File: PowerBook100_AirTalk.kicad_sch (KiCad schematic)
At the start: 41 parts, among them J1 5-104652-2, J2 PRG_HDR, Q1 BSS138, SW1 RST, U1 TashTalk, U2 TXB0104PWR, U3 AMS1117-3.3, U4 ESP32-WROOM-32DM113DH6400PH3Q0, U5 74LVC2G125

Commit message: More mods
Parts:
- removed TP1: RX_PB, TestPoint:TestPoint_Pad_2.0x2.0mm, symbol Connector:TestPoint
- removed TP2: TX_PB, TestPoint:TestPoint_Pad_2.0x2.0mm, symbol Connector:TestPoint
- removed TP3: RTS_PB, TestPoint:TestPoint_Pad_2.0x2.0mm, symbol Connector:TestPoint
- added R17, R18, R19: 0, Resistor_SMD:R_0805_2012Metric, symbol Device:R
- C1, C11, C2, C3, C4, C5, C7: footprint Capacitor_SMD:CP_Elec_6.3x7.7 -> Capacitor_SMD:C_1206_3216Metric
- J2: footprint Connector_Samtec_HPM_THT:Samtec_HPM-03-01-x-S_Straight_1x03_Pitch5.08mm -> Connector_PinHeader_2.00mm:PinHeader_1x03_P2.00mm_Vertical_SMD_Pin1Right
- R12: value 0 -> R
- U1: footprint Package_DIP:DIP-8_W7.62mm -> Package_SO:SOIC-8-1EP_3.9x4.9mm_P1.27mm_EP2.29x3mm
- U3: footprint Package_TO_SOT_SMD:SOT-223-3_TabPin2 -> Package_TO_SOT_SMD:TO-252-3_TabPin2
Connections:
- net +3.3V: now also R12.1
- net +5V: now also R17.2, R18.2; no longer J1.5, R12.1
- net LT_TX_33: now also R12.2
- net MODEM_INSERT: no longer R12.2
- net PB_CTS: now reaches J1.14
- net PB_CTS: now also R19.1
- net MODEM_5v: now reaches J1.18
- net MODEM_5v: now also J1.20, R17.1
- net at R11.2, U2.5 (A4): now also R19.2
- new net ALWAYS_ON_5V: J1.5, R18.1
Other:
- note added: "Puoi usare SOIC8"
- moved on the sheet: R11

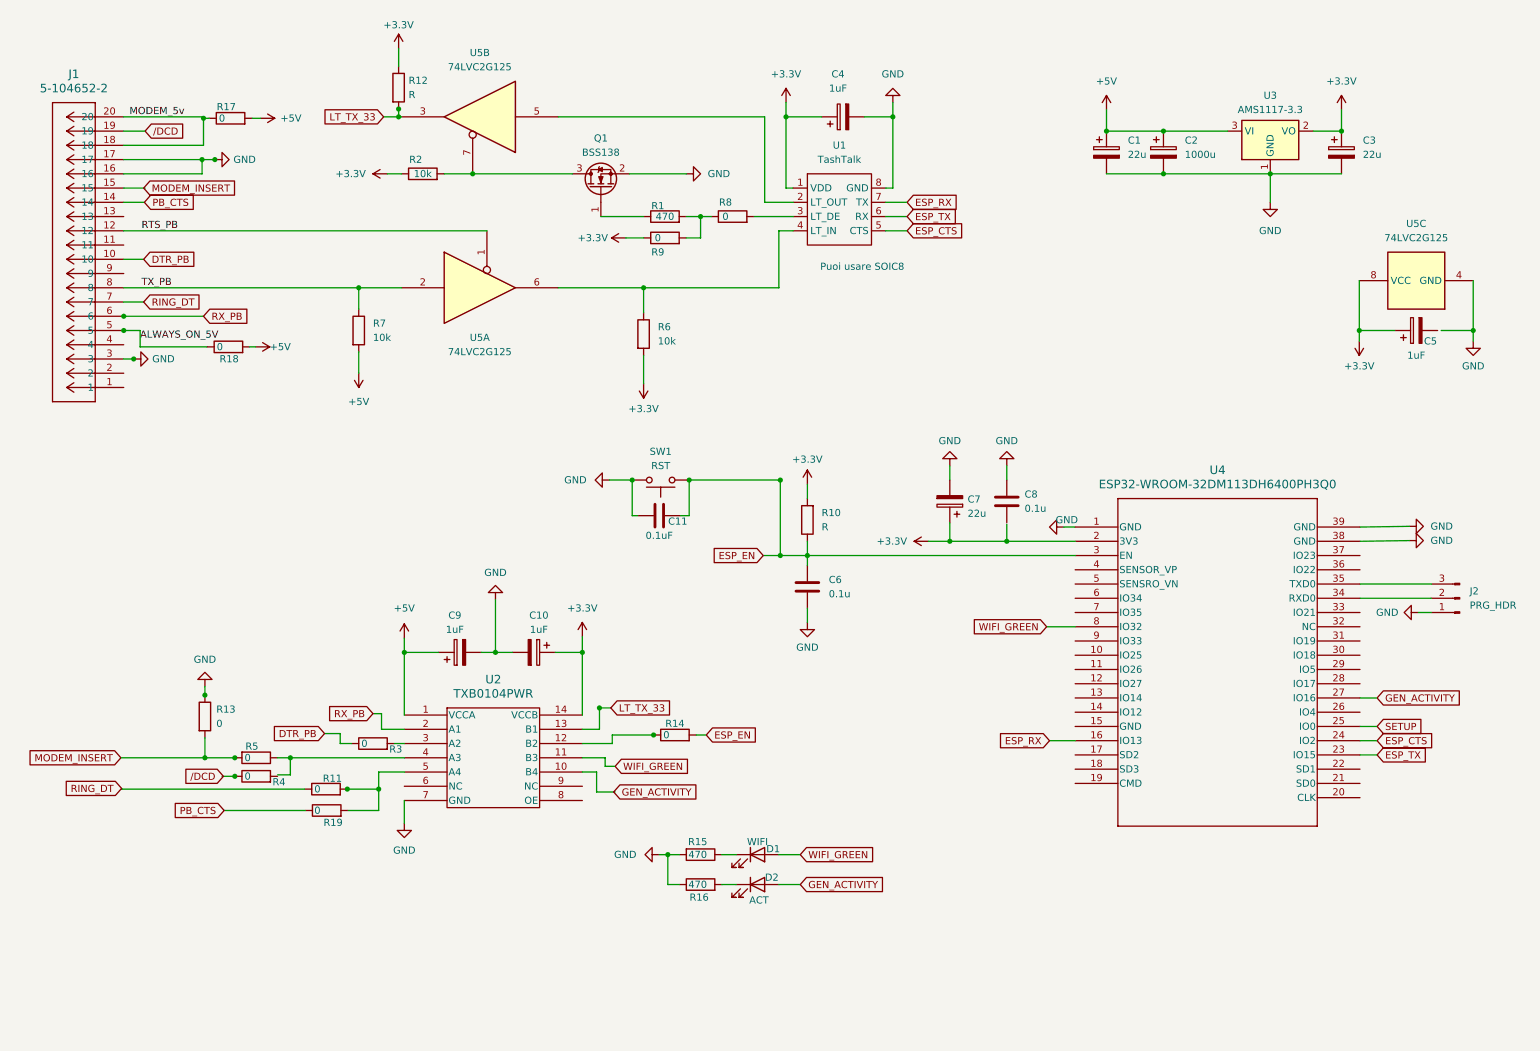
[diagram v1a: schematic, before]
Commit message: Add PCB layout
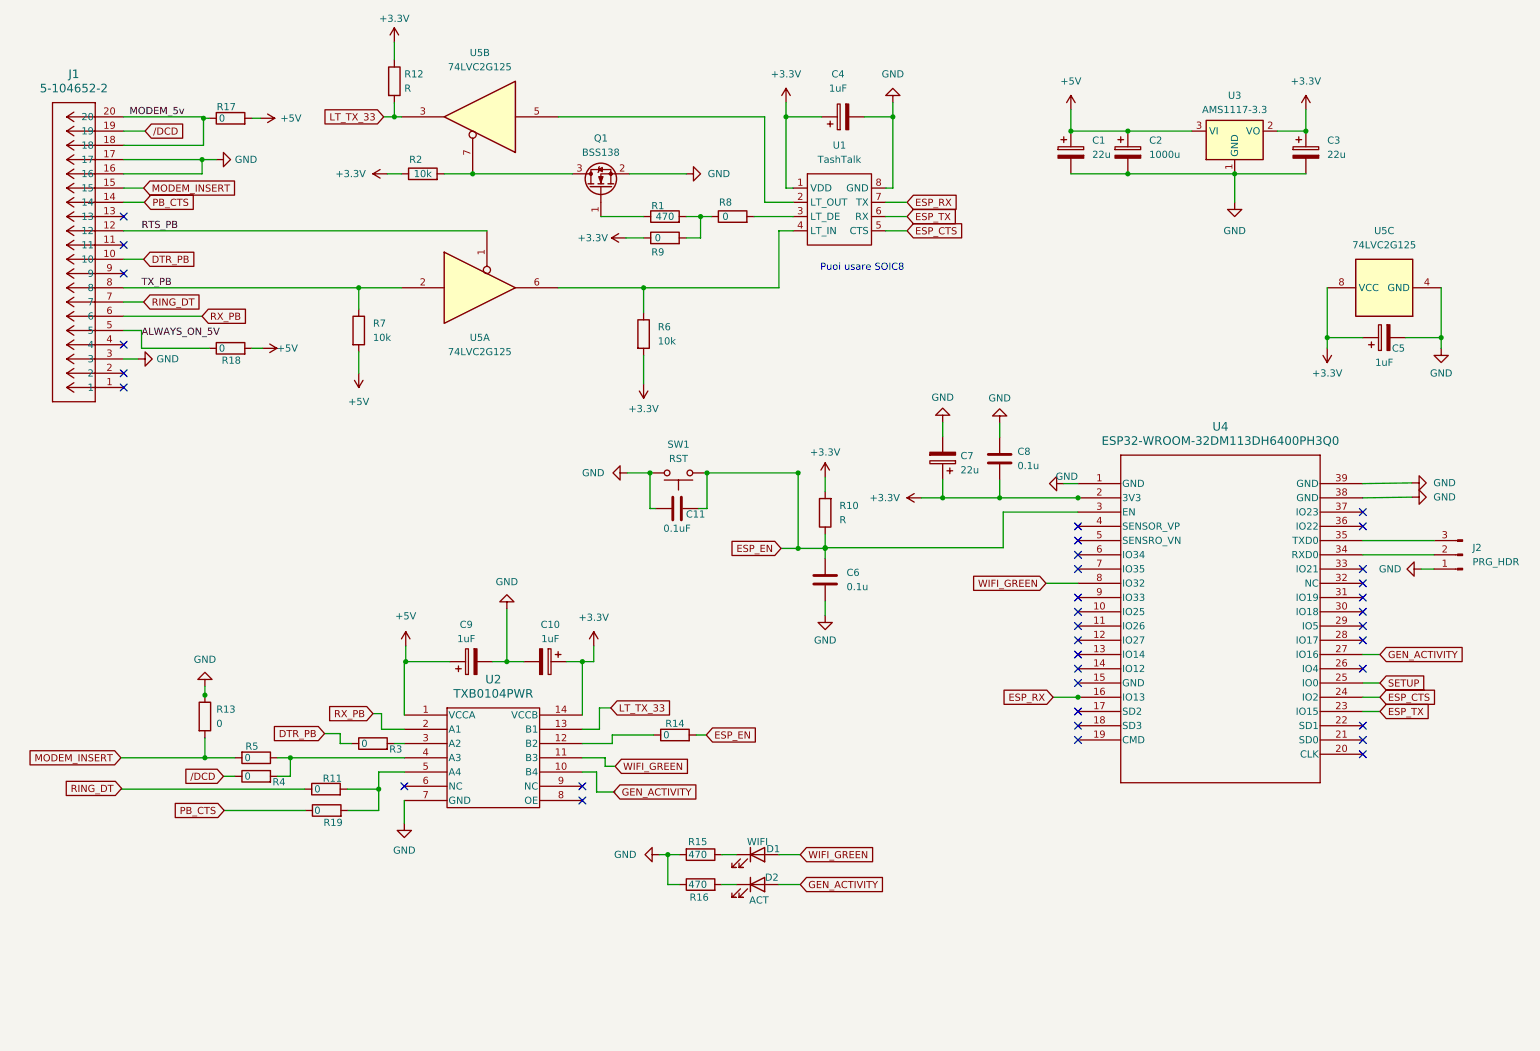
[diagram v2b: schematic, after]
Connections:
- net +3.3V: now also C8.2
- net GND: now also C5.2
- net at R5.1, U2.4 (A3): now also R4.2
- no-connect marks 0 -> 35
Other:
- moved on the sheet: C1, C10, C11, C2, C3, C5, C6, C7, C8, C9, J2, R10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

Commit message: New revision
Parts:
- removed C1, C3: 22u, Capacitor_SMD:C_1206_3216Metric, symbol Device:C_Polarized
- removed C10, C9: 1uF, Capacitor_SMD:C_0805_2012Metric, symbol Device:C_Polarized
- removed C2: 1000u, Capacitor_SMD:C_1206_3216Metric, symbol Device:C_Polarized
- removed J2: PRG_HDR, Connector_PinHeader_2.00mm:PinHeader_1x03_P2.00mm_Vertical_SMD_Pin1Right, symbol Connector:Conn_01x03_Pin
- removed R1: 470, Resistor_SMD:R_0805_2012Metric, symbol Device:R
- removed R13, R14, R17, R18, R19: 0, Resistor_SMD:R_0805_2012Metric, symbol Device:R
- removed SW1: RST, Button_Switch_SMD:SW_SPST_EVPBF, symbol Switch:SW_Push
- removed U2: TXB0104PWR, Package_SO:HTSSOP-14-1EP_4.4x5mm_P0.65mm_EP3.4x5mm_Mask3x3.1mm, symbol 2023-07-31_10-22-16:TXB0104PWR
- added C1: 10uF, Capacitor_SMD:C_0805_2012Metric, symbol Device:C
- added C10, C9: 0.1uF, Capacitor_SMD:C_0805_2012Metric, symbol Device:C
- added C12: 0.1uF, Capacitor_SMD:C_1206_3216Metric, symbol Device:C
- added C2: 22uF, Capacitor_SMD:C_0805_2012Metric, symbol Device:C
- added D3: 3.3V, LED_SMD:LED_0805_2012Metric, symbol Device:LED
- added D4: 5V, LED_SMD:LED_0805_2012Metric, symbol Device:LED
- added J2: PRG, Connector_PinHeader_1.00mm:PinHeader_1x04_P1.00mm_Vertical_SMD_Pin1Right, symbol Connector_Generic:Conn_01x04
- added R20, R21: 10K, Resistor_SMD:R_0805_2012Metric, symbol Device:R
- added SW1, SW2: TS-1187A-B-A-B, Button_Switch_SMD:SW_Push_1P1T_XKB_TS-1187A, symbol 2023-10-14_07-33-24:TS-1187A-B-A-B
- added U6: TXU0304PWR, footprints:TSSOP14_PW_TEX, symbol 2023-10-16_16-52-45:TXU0304PWR
- C6, C8: value 0.1u -> 0.1uF
- C7: value 22u -> 22uF
- R10, R12: value R -> 10K
- R3: value 0 -> 470
- R4: value 0 -> 10K
- R5: value 0 -> 1K
- U1: footprint Package_SO:SOIC-8-1EP_3.9x4.9mm_P1.27mm_EP2.29x3mm -> Package_SO:SOIC-8_3.9x4.9mm_P1.27mm
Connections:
- net MODEM_5v is gone; now on net +5V: J1.18, J1.20
- net +3.3V: now also C10.1, C2.1, D3.2 (A), J2.4 (Pin_4), R20.2, U6.1 (VCCA)
- net +5V: now also C1.1, C9.1, D4.2 (A), R21.2, U6.14 (VCCB), U6.8 (OE)
- net DTR_PB: now also U6.10 (B4); no longer R3.1
- net ESP_EN: now also R11.2, SW1.2; no longer C11.2
- net GEN_ACTIVITY: now also U6.2 (A1)
- net GND: now also J1.11, R3.1, R4.2, R5.1, U4.15 (GND), C1.2, C10.2, C2.2, C9.2, J2.3 (Pin_3), SW1.4, SW2.4, U6.7 (GND); no longer C11.1
- net LT_TX_33: now also U6.4 (A3)
- net PB_CTS: now also U6.13 (B1Y)
- net RING_DT: no longer R11.1
- net RX_PB: now also U6.11 (B3Y)
- net SETUP: now also R20.1, SW2.2
- net WIFI_GREEN: now also U6.3 (A2)
- net /DCD: now also U6.12 (B2Y); no longer R4.1
- net MODEM_PWR: now reaches J1.2
- net MODEM_PWR: now also R21.1
- net at R3.2: now also D3.1 (K)
- net at R8.1, R9.2: now also Q1.1 (G)
- net at U4.34 (RXD0): now also J2.2 (Pin_2)
- net at U4.35 (TXD0): now also J2.1 (Pin_1)
- net ALWAYS_ON_5V: no longer names the net of J1.5
- net MODEM_INSERT: no longer names the net of R5.2
- net MODEM_INSERT: now also D4.1 (K); no longer J1.15
- new net: C12.1, SW2.1
- new net: C12.2, SW2.3
- new net: R11.1, U6.5 (A4Y)
- new net: C11.2, SW1.1
- new net: C11.1, SW1.3
- new net MODEM_INS: J1.15, R4.1
- no-connect marks 35 -> 25
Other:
- note added: "2N7002"
- note added: "AZ1117CD-3.3TRG1"
- note added: "App. note requires 10K pullup between MODEM.PWR and MODEM.5V"
- note added: "Ceramic cap for AZ1117C"
- note added: "Digikey"
- moved on the sheet: C11, D1, D2, R15, R16
